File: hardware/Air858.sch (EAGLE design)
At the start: 56 parts, among them IC1 ATMEGA168, IC2 MAX31855, IC3 LD117, Q1 TSM3404, SW1 EC12E_SW, T1 BTA16, X1 CSTCR6M00G53Z

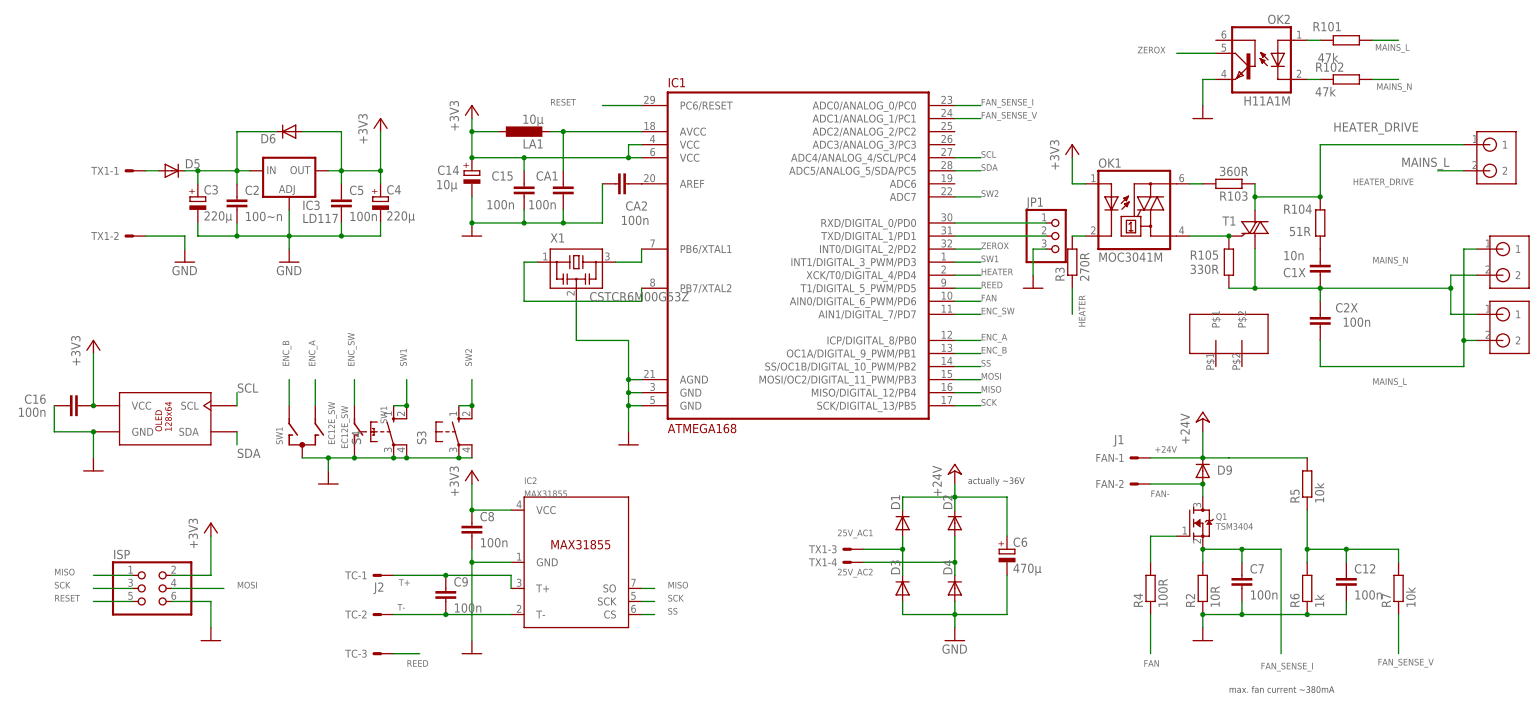
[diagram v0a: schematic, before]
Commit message: changed zero crossing detection based on AVR182
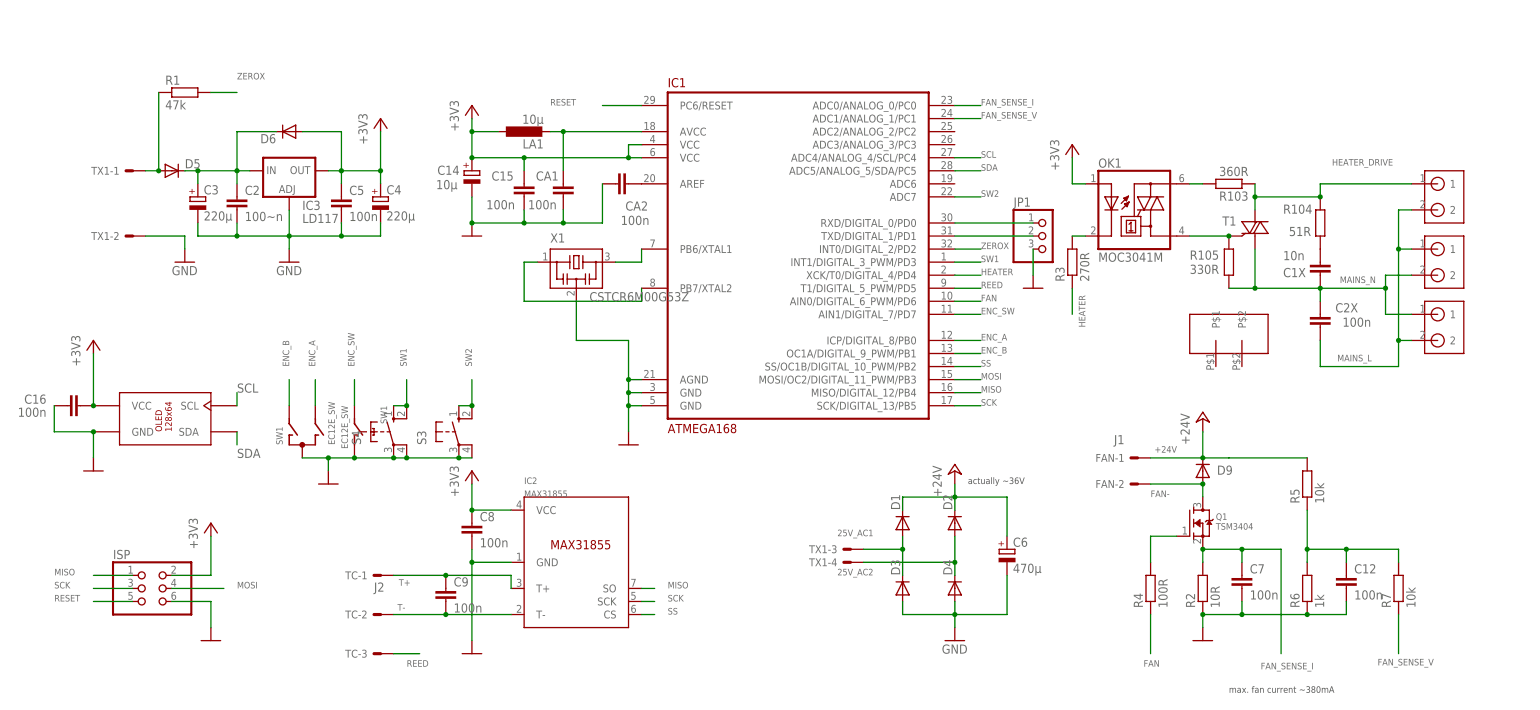
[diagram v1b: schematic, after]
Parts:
- removed OK2: H11A1M, optocoupler:H11A1M
- removed R101, R102: 47k, rcl:R-EU_M1206
- added R1: 47k, rcl:R-EU_R0603
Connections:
- removed net N$2: OK2.A, R101.2
- removed net N$7: OK2.C, R102.2
- net 10V_AC1: now also R1.1
- net GND: no longer OK2.EMI
- net MAINS_L: no longer R101.1
- net MAINS_N: no longer R102.1
- net ZEROX: now also R1.2; no longer OK2.COL
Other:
- moved on the sheet: JP1
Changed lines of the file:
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@@
 <part name="GND10" library="supply1" deviceset="GND" device=""/>
 <part name="C16" library="rcl" deviceset="C-EU" device="C0603K" value="100n"/>
-<part name="OK2" library="optocoupler" deviceset="H11A*?M" device="" technology="1"/>
-<part name="R101" library="rcl" deviceset="R-EU_" device="M1206" value="47k"/>
-<part name="R102" library="rcl" deviceset="R-EU_" device="M1206" value="47k"/>
-<part name="GND11" library="supply1" deviceset="GND" device=""/>
 <part name="LA1" library="rcl" deviceset="L-EU" device="L3225P" value="10µ"/>
 <part name="CA1" library="rcl" deviceset="C-EU" device="C0603K" value="100n"/>
@@
 <part name="U$5" library="pit" deviceset="HEATSINK17X7.5TO220" device=""/>
 <part name="X1" library="murata-filter" deviceset="CSTCR" device="" technology="6M00G53Z"/>
+<part name="R1" library="rcl" deviceset="R-EU_" device="R0603" value="47k"/>
 </parts>
 <sheets>
@@
 <attribute name="VALUE" x="-47.244" y="9.779" size="1.778" layer="96" rot="R180"/>
 </instance>
-<instance part="OK2" gate="G$1" x="187.96" y="78.74" rot="MR0"/>
-<instance part="R101" gate="G$1" x="205.74" y="81.28" smashed="yes" rot="R180">
-<attribute name="NAME" x="199.136" y="83.0326" size="1.778" layer="95"/>
-<attribute name="VALUE" x="200.152" y="76.962" size="1.778" layer="96"/>
-</instance>
-<instance part="R102" gate="G$1" x="205.74" y="73.66" smashed="yes" rot="R180">
-<attribute name="NAME" x="199.644" y="75.1586" size="1.778" layer="95"/>
-<attribute name="VALUE" x="199.644" y="70.358" size="1.778" layer="96"/>
-</instance>
-<instance part="GND11" gate="1" x="177.8" y="66.04" smashed="yes"/>
 <instance part="LA1" gate="G$1" x="45.72" y="63.5" smashed="yes" rot="R90">
 <attribute name="NAME" x="49.53" y="62.0014" size="1.778" layer="95" rot="R180"/>
@@
 <instance part="S3" gate="1" x="33.02" y="5.08"/>
 <instance part="S4" gate="1" x="20.32" y="5.08"/>
-<instance part="JP1" gate="A" x="149.86" y="43.18"/>
+<instance part="JP1" gate="A" x="147.32" y="43.18"/>
 <instance part="GND12" gate="1" x="144.78" y="33.02" smashed="yes"/>
-<instance part="HEATER" gate="G$1" x="233.68" y="58.42" rot="R270"/>
-<instance part="MAINS1" gate="G$1" x="236.22" y="38.1" rot="R270"/>
-<instance part="MAINS2" gate="G$1" x="236.22" y="25.4" rot="R270"/>
+<instance part="HEATER" gate="G$1" x="223.52" y="50.8" rot="R270"/>
+<instance part="MAINS1" gate="G$1" x="223.52" y="38.1" rot="R270"/>
+<instance part="MAINS2" gate="G$1" x="223.52" y="25.4" rot="R270"/>
 <instance part="U$5" gate="G$1" x="182.88" y="22.86"/>
 <instance part="X1" gate="G$1" x="55.88" y="38.1"/>
+<instance part="R1" gate="G$1" x="-20.32" y="71.12"/>
 </instances>
 <busses>
@@
 </segment>
 <segment>
-<pinref part="OK2" gate="G$1" pin="EMI"/>
-<pinref part="GND11" gate="1" pin="GND"/>
-<wire x1="180.34" y1="73.66" x2="177.8" y2="73.66" width="0.1524" layer="91"/>
-<wire x1="177.8" y1="73.66" x2="177.8" y2="68.58" width="0.1524" layer="91"/>
-</segment>
-<segment>
 <pinref part="CA1" gate="G$1" pin="2"/>
 <wire x1="53.34" y1="48.26" x2="53.34" y2="45.72" width="0.1524" layer="91"/>
@@
 <pinref part="GND12" gate="1" pin="GND"/>
 <wire x1="144.78" y1="35.56" x2="144.78" y2="40.64" width="0.1524" layer="91"/>
-<wire x1="144.78" y1="40.64" x2="147.32" y2="40.64" width="0.1524" layer="91"/>
 </segment>
 </net>
@@
 <pinref part="TX1" gate="-1" pin="S"/>
 <wire x1="-27.94" y1="55.88" x2="-25.4" y2="55.88" width="0.1524" layer="91"/>
+<pinref part="R1" gate="G$1" pin="1"/>
+<wire x1="-25.4" y1="55.88" x2="-25.4" y2="71.12" width="0.1524" layer="91"/>
+<junction x="-25.4" y="55.88"/>
 </segment>
 </net>
@@
 <junction x="187.96" y="50.8"/>
 <junction x="200.66" y="50.8"/>
-<label x="207.01" y="53.086" size="1.27" layer="95"/>
-<wire x1="200.66" y1="50.8" x2="200.66" y2="60.96" width="0.1524" layer="91"/>
+<label x="202.946" y="56.896" size="1.27" layer="95"/>
+<wire x1="200.66" y1="50.8" x2="200.66" y2="53.34" width="0.1524" layer="91"/>
 <pinref part="HEATER" gate="G$1" pin="1"/>
-<wire x1="200.66" y1="60.96" x2="228.6" y2="60.96" width="0.1524" layer="91"/>
-<label x="203.2" y="63.5" size="1.778" layer="95"/>
+<wire x1="200.66" y1="53.34" x2="218.44" y2="53.34" width="0.1524" layer="91"/>
 </segment>
 </net>
@@
 <junction x="187.96" y="33.02"/>
 <junction x="200.66" y="33.02"/>
-<label x="210.82" y="37.846" size="1.27" layer="95"/>
+<label x="204.47" y="34.036" size="1.27" layer="95"/>
 <pinref part="MAINS1" gate="G$1" pin="2"/>
-<wire x1="231.14" y1="35.56" x2="226.06" y2="35.56" width="0.1524" layer="91"/>
-<wire x1="226.06" y1="35.56" x2="226.06" y2="33.02" width="0.1524" layer="91"/>
+<wire x1="218.44" y1="35.56" x2="213.36" y2="35.56" width="0.1524" layer="91"/>
+<wire x1="213.36" y1="35.56" x2="213.36" y2="33.02" width="0.1524" layer="91"/>
 <pinref part="MAINS2" gate="G$1" pin="1"/>
-<wire x1="226.06" y1="33.02" x2="226.06" y2="27.94" width="0.1524" layer="91"/>
-<wire x1="226.06" y1="27.94" x2="231.14" y2="27.94" width="0.1524" layer="91"/>
-<wire x1="200.66" y1="33.02" x2="226.06" y2="33.02" width="0.1524" layer="91"/>
-<junction x="226.06" y="33.02"/>
-</segment>
-<segment>
-<pinref part="R102" gate="G$1" pin="1"/>
-<wire x1="210.82" y1="73.66" x2="215.9" y2="73.66" width="0.1524" layer="91"/>
-<label x="211.582" y="71.628" size="1.27" layer="95"/>
+<wire x1="213.36" y1="33.02" x2="213.36" y2="27.94" width="0.1524" layer="91"/>
+<wire x1="213.36" y1="27.94" x2="218.44" y2="27.94" width="0.1524" layer="91"/>
+<wire x1="200.66" y1="33.02" x2="213.36" y2="33.02" width="0.1524" layer="91"/>
+<junction x="213.36" y="33.02"/>
 </segment>
 </net>
@@
 <pinref part="C2X" gate="G$1" pin="1"/>
 <wire x1="200.66" y1="17.78" x2="200.66" y2="22.86" width="0.1524" layer="91"/>
-<label x="210.82" y="14.224" size="1.27" layer="95"/>
+<label x="203.962" y="18.796" size="1.27" layer="95"/>
 <pinref part="MAINS1" gate="G$1" pin="1"/>
-<wire x1="231.14" y1="40.64" x2="228.6" y2="40.64" width="0.1524" layer="91"/>
-<wire x1="228.6" y1="40.64" x2="228.6" y2="22.86" width="0.1524" layer="91"/>
+<wire x1="218.44" y1="40.64" x2="215.9" y2="40.64" width="0.1524" layer="91"/>
+<wire x1="215.9" y1="40.64" x2="215.9" y2="22.86" width="0.1524" layer="91"/>
 <pinref part="MAINS2" gate="G$1" pin="2"/>
-<wire x1="228.6" y1="22.86" x2="231.14" y2="22.86" width="0.1524" layer="91"/>
-<wire x1="200.66" y1="17.78" x2="228.6" y2="17.78" width="0.1524" layer="91"/>
-<wire x1="228.6" y1="17.78" x2="228.6" y2="22.86" width="0.1524" layer="91"/>
-<junction x="228.6" y="22.86"/>
-</segment>
-<segment>
-<pinref part="R101" gate="G$1" pin="1"/>
-<wire x1="210.82" y1="81.28" x2="215.9" y2="81.28" width="0.1524" layer="91"/>
-<label x="211.328" y="79.248" size="1.27" layer="95"/>
-</segment>
-<segment>
+<wire x1="215.9" y1="22.86" x2="218.44" y2="22.86" width="0.1524" layer="91"/>
+<wire x1="200.66" y1="17.78" x2="215.9" y2="17.78" width="0.1524" layer="91"/>
+<wire x1="215.9" y1="17.78" x2="215.9" y2="22.86" width="0.1524" layer="91"/>
+<junction x="215.9" y="22.86"/>
 <pinref part="HEATER" gate="G$1" pin="2"/>
-<wire x1="228.6" y1="55.88" x2="223.52" y2="55.88" width="0.1524" layer="91"/>
-<label x="216.408" y="56.642" size="1.778" layer="95"/>
+<wire x1="218.44" y1="48.26" x2="215.9" y2="48.26" width="0.1524" layer="91"/>
+<wire x1="215.9" y1="48.26" x2="215.9" y2="40.64" width="0.1524" layer="91"/>
+<junction x="215.9" y="40.64"/>
 </segment>
 </net>
@@
 <net name="ZEROX" class="0">
 <segment>
-<pinref part="OK2" gate="G$1" pin="COL"/>
-<wire x1="180.34" y1="78.74" x2="172.72" y2="78.74" width="0.1524" layer="91"/>
-<label x="165.1" y="78.74" size="1.27" layer="95"/>
+<wire x1="-10.16" y1="71.12" x2="-15.24" y2="71.12" width="0.1524" layer="91"/>
+<label x="-10.16" y="73.66" size="1.27" layer="95"/>
+<pinref part="R1" gate="G$1" pin="2"/>
 </segment>
 <segment>
@@
 <pinref part="IC1" gate="G$1" pin="RXD/DIGITAL_0/PD0"/>
 <pinref part="JP1" gate="A" pin="1"/>
-<wire x1="129.54" y1="45.72" x2="147.32" y2="45.72" width="0.1524" layer="91"/>
+<wire x1="129.54" y1="45.72" x2="144.78" y2="45.72" width="0.1524" layer="91"/>
 </segment>
 </net>
@@
 <pinref part="IC1" gate="G$1" pin="TXD/DIGITAL_1/PD1"/>
 <pinref part="JP1" gate="A" pin="2"/>
-<wire x1="129.54" y1="43.18" x2="147.32" y2="43.18" width="0.1524" layer="91"/>
-</segment>
-</net>
-<net name="N$2" class="0">
-<segment>
-<pinref part="OK2" gate="G$1" pin="A"/>
-<pinref part="R101" gate="G$1" pin="2"/>
-<wire x1="198.12" y1="81.28" x2="200.66" y2="81.28" width="0.1524" layer="91"/>
-</segment>
-</net>
-<net name="N$7" class="0">
-<segment>
-<pinref part="R102" gate="G$1" pin="2"/>
-<pinref part="OK2" gate="G$1" pin="C"/>
-<wire x1="200.66" y1="73.66" x2="198.12" y2="73.66" width="0.1524" layer="91"/>
-</segment>
-</net>
+<wire x1="129.54" y1="43.18" x2="144.78" y2="43.18" width="0.1524" layer="91"/>
+</segment>
+</net>
